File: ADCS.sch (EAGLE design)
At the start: 183 parts, among them U1 Value, U2 Value, U3 Value, U34 TMP100, U4 Value, U5 TEXAS_INSTRUMENTS-AND_GATE-SN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, U6 ISSI-DRAM-IS42S16320F-7TL, U7 TMP100, U8 BMX160, U9 BMX160, X1 ECS_INC-OSCILLATOR-ECS-400-10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, X2 BU-SMA-V, X3 2510-, X4 2510-, Y1 20MHz, Y2 20MHz

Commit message: Almost done with schematic
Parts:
- added C143, C144, C145, C146, C147, C148, C149, C150, C151, C152, C153, C154, C155, C156, C159, C162, C163, C165, C166, C168, C170, C172, C174, C175, C176, C177, C178, C179, C180, C181, C185, C187: 0.1uF, standardparts:CAPACITOR.0603
- added C157, C160, C167, C169: 2.2uF, standardparts:CAPACITOR.0603
- added C158, C161, C164: 10uF, standardparts:CAPACITOR.0805
- added C171, C173, C182, C186, C188: 1uF, standardparts:CAPACITOR.0603
- added C183: 4.7uF, standardparts:CAPACITOR.0603
- added C184: (no value), standardparts:CAPACITOR.0603
- added C189: 10nF, standardparts:CAPACITOR.0603
- added IC1: XC9572XL-10VQG44C, SamacSys_Parts:XC9572XL-10VQG44C
- added J1: SEAF-10-XX.X-XX-04-X-A, SEAF-10-XX.X-XX-04-X-A:SEAF-10-XX.X-XX-04-X-A
- added JP1, JP4: (no value), pinhead:PINHD-1X8
- added JP5, JP6, JP7, JP8: (no value), pinhead:PINHD-1X2
- added JP9: (no value), pinhead:PINHD-1X4
- added R13, R21, R30, R32, R40, R62, R63: 10k, standardparts:RESISTOR.0603
- added R14, R22, R42: (no value), standardparts:RESISTOR.0603
- added R15, R16, R17, R18, R23, R24, R25, R26, R37, R39, R44, R45, R46, R47, R48, R49, R50, R51, R53, R54, R55, R56, R57, R58, R59, R60: DNI, standardparts:RESISTOR.0603
- added R19, R20, R27, R28: 1R_1%, standardparts:RESISTOR.0603
- added R29, R31: (no value), standardparts:RESISTOR.1206
- added R36, R38, R52, R61: 4.7k, standardparts:RESISTOR.0603
- added R41: 120R, standardparts:RESISTOR.0603
- added R43: 1M, standardparts:RESISTOR.0603
- added U10, U11: Value, Module_ICs:TEXAS_INSTRUMENTS-MOTOR_PWM_DRIVER-DRV8833CPWP
- added U12, U13: TEXAS_INSTRUMENTS-CURRENT_MONITOR-INA226_DGS_10, Module_Regulators:TEXAS_INSTRUMENTS-CURRENT_MONITOR-INA226_DGS_10
- added U14: Value, Module_ICs:TEXAS_INSTRUMENTS-CAN_TRANSCEIVER-TCAN1042VDRQ1
- added U15, U16: KIOXIA_AMERICA-NAND_FLASH-TC58CVG0S3HRAIG, Module_ICs:KIOXIA_AMERICA-NAND_FLASH-TC58CVG0S3HRAIG
- added X5: 2510-, con-3m:2510-
- R4: value 10k -> 4.7k
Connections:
- removed net I2C0_SCL: U34.SCL, U7.SCL, U8.SCX, U9.SCX
- removed net I2C0_SDA: U34.SDA, U7.SDA, U8.SDX, U9.SDX
- new net !ADCS_FAILURE: C184.1, IC1.I/O_1, R42.2
- new net !COMMS1_ERROR: IC1.I/O_9
- new net !COMMS1_NAND_CS: U15.!CS, U3.PF3
- new net !COMMS1_RESET: IC1.I/O_3
- new net !COMMS1_UNRESPONSIVE: IC1.I/O_11, R62.2, U2D.GPIO20
- new net !COMMS2_ERROR: IC1.I/O_10
- new net !COMMS2_RESET: IC1.I/O_4
- new net !COMMS2_UNRESPONSIVE: IC1.I/O_12, R63.2, U2D.GPIO21
- new net !COMMS_ERROR: R61.2, U3.PD6
- new net !MTQ12_FAULT: R14.2, U10.FAULT_N
- new net !MTQ12_SLEEP: R13.2, U10.SLEEP_N
- new net !MTQ34_FAULT: R22.2, U11.FAULT_N
- new net !MTQ34_SLEEP: R21.2, U11.SLEEP_N
- new net !SMC_NAND_CS: U16.!CS, U2D.GPIO19
- new net ADCS_ERROR: IC1.I/O_6, J1G$3.10
- new net ADCS_FAILURE: J1G$1.10
- new net ADCS_ONLINE: IC1.I/O_5, J1G$3.9
- new net ADC_A0: C149.1, JP1.2, U2B.ADCINA0_DACOUTA
- new net ADC_A1: C148.1, JP1.3, U2B.ADCINA1_DACOUTB
- new net ADC_A2: C147.1, JP1.4, U2B.ADCINA2_CMPIN1P
- new net ADC_A3: C146.1, JP1.5, U2B.ADCINA3_CMPIN1N
- new net ADC_A4: C145.1, JP1.6, U2B.ADCINA4_CMPIN2P
- new net ADC_A5: C144.1, JP1.7, U2B.ADCINA5_CMPIN2N
- new net ADC_B0: C156.1, JP4.2, U2B.ADCINB0_VDAC
- new net ADC_B1: C155.1, JP4.3, U2B.ADCINB1_DACOUTC
- new net ADC_B2: C154.1, JP4.4, U2B.ADCINB2_CMPIN3P
- new net ADC_B3: C153.1, JP4.5, U2B.ADCINB3_CMPIN3N
- new net ADC_B4: C152.1, JP4.6, U2B.ADCINB4
- new net ADC_B5: C151.1, JP4.7, U2B.ADCINB5
- new net COMMS1_NAND_MISO: U15.SO/SO1, U3.PF0
- new net COMMS1_NAND_MOSI: U15.SI/SO0, U3.PF1
- new net COMMS1_NAND_SCK: U15.SCK, U3.PF2
- new net COMMS1_NMI: C189.1, IC1.I/O_7, R52.1, U3.PD7
- new net COMMS2_NMI: IC1.I/O_8
- new net COMMS2_UART_RX: J1G$3.8
- new net COMMS2_UART_TX: J1G$3.7
- new net CPLD_I1: IC1.I/O/GTS1, J1G$4.3
- new net CPLD_I2: IC1.I/O_23, J1G$4.4
- new net CPLD_I3: IC1.I/O_24, J1G$4.5
- new net CPLD_I4: IC1.I/O_25, J1G$4.6
- new net CPLD_O1: IC1.I/O_26, J1G$4.7
- new net CPLD_O2: IC1.I/O_27, J1G$4.8
- new net CPLD_O3: IC1.I/O_28, J1G$4.9
- new net CPLD_O4: IC1.I/O/GCK1, J1G$4.10
- new net EPWM1A: R18.1, U10.AIN1, U2D.GPIO0
- new net EPWM1B: R17.1, U10.AIN2, U2D.GPIO1
- new net EPWM2A: R16.1, U10.BIN1, U2D.GPIO2
- new net EPWM2B: R15.1, U10.BIN2, U2D.GPIO3
- new net EPWM3A: R26.1, U11.AIN1, U2D.GPIO4
- new net EPWM3B: R25.1, U11.AIN2, U2D.GPIO5
- new net EPWM4A: R24.1, U11.BIN1, U2D.GPIO6
- new net EPWM4B: R23.1, U11.BIN2, U2D.GPIO7
- new net MTQ1_OUT1: JP5.1, U10.AOUT1
- new net MTQ1_OUT2: JP5.2, U10.AOUT2
- new net MTQ2_OUT1: JP6.1, U10.BOUT1
- new net MTQ2_OUT2: JP6.2, U10.BOUT2
- new net MTQ3_OUT1: JP7.1, U11.AOUT1
- new net MTQ3_OUT2: JP7.2, U11.AOUT2
- new net MTQ4_OUT1: JP8.1, U11.BOUT1
- new net MTQ4_OUT2: JP8.2, U11.BOUT2
- new net MTQ_12_ALERT: R32.2, U13.ALERT
- new net MTQ_12_VCC: C158.1, C159.1, C164.1, C165.1, R31.2, U10.VM, U13.VIN-
- new net MTQ_34_ALERT: R30.2, U12.ALERT
- new net MTQ_34_VCC: C161.1, C162.1, R29.2, U11.VM, U12.VIN-
- new net N$10: C157.1, U10.VINT
- new net N$12: R19.1, U10.AISEN
- new net N$13: R20.1, U10.BISEN
- new net N$14: C160.1, U11.VINT
- new net N$15: R27.1, U11.AISEN
- new net N$16: R28.1, U11.BISEN
- new net N$17: R44.2, R45.1, U15.!WP!/SO2
- new net N$18: IC1.TMS, X5-2.KL
- new net N$19: IC1.TCK, X5-4.KL
- new net N$29: IC1.TDI, X5-8.KL
- new net N$30: IC1.TDO, X5-6.KL
- new net N$37: R48.2, R49.1, U16.!WP!/SO2
- new net N$38: R46.2, R47.1, U15.!HOLD!/SO3
- new net N$39: R50.2, R51.1, U16.!HOLD!/SO3
- new net SMC_ERR_OUT_CPLD: IC1.I/O_2, R43.2
- new net SMC_I2C0_SCL: J1G$1.2, R37.2, U12.SCL, U13.SCL, U2F.GPIO105, U34.SCL, U7.SCL, U8.SCX, U9.SCX
- new net SMC_I2C0_SDA: J1G$1.1, R36.2, U12.SDA, U13.SDA, U2F.GPIO104, U34.SDA, U7.SDA, U8.SDX, U9.SDX
- new net SMC_I2C1_SCL: J1G$1.5, R39.2, U2D.GPIO41
- new net SMC_I2C1_SDA: J1G$1.4, R38.2, U2D.GPIO40
- new net SMC_MCAN_RX: U14.RXD, U2D.GPIO10
- new net SMC_MCAN_STB: R40.1, U14.STB, U2D.GPIO9
- new net SMC_MCAN_TX: U14.TXD, U2D.GPIO8
- new net SMC_NAND_MISO: U16.SO/SO1, U2D.GPIO17
- new net SMC_NAND_MOSI: U16.SI/SO0, U2D.GPIO16
- new net SMC_NAND_SCK: U16.SCK, U2D.GPIO18
- new net SMC_UART0_RX: J1G$3.2, JP9.3, U2E.GPIO43
- new net SMC_UART0_TX: J1G$3.1, JP9.2, U2E.GPIO42
- net !GLOBAL_RESET: now also IC1.I/O/GCK2
- net BMX160_1_INT1: now also R54.2, R55.1, U2D.GPIO11
- net BMX160_1_INT2: now also R53.2, R56.1, U2D.GPIO12
- net BMX160_2_INT1: now also R58.2, R59.1, U2D.GPIO13
- net BMX160_2_INT2: now also R57.2, R60.1, U2D.GPIO14
- net CANH: now also J1G$1.7, R41.1, U14.CANH
- net CANL: now also J1G$1.8, R41.2, U14.CANL
- net COMMS1_UART_RX: now also J1G$3.5
- net COMMS1_UART_TX: now also J1G$3.4
- net SMC_ERR_OUT: now also R43.1
- net VCC_3V3_IO: now also C143.1, C150.1, C163.1, C166.1, C167.1, C170.1, C171.1, C172.1, C175.1, C176.1, C177.1, C178.1, C179.1, C180.1, C181.1, C182.1, C183.1, C185.1, C186.1, C187.1, C188.1, IC1.VCCINT_3.3V_1, IC1.VCCINT_3.3V_2, IC1.VCCIO_2.5V/3.3V, J1G$2.3, J1G$2.4, JP1.1, JP4.1, JP9.1, R13.1, R14.1, R21.1, R22.1, R30.1, R32.1, R36.1, R37.1, R38.1, R39.1, R42.1, R44.1, R46.1, R48.1, R50.1, R53.1, R54.1, R57.1, R58.1, R61.1, R62.1, R63.1, U12.VS, U13.A0, U13.VS, U14.VIO, U15.VCC, U16.VCC, X5-1.KL
- net VCC_5V0: now also C168.1, C169.1, C173.1, C174.1, J1G$2.1, J1G$2.2, R29.1, R31.1, U12.VBUS, U12.VIN+, U13.VBUS, U13.VIN+, U14.VCC
- net VSS: now also C143.2, C144.2, C145.2, C146.2, C147.2, C148.2, C149.2, C150.2, C151.2, C152.2, C153.2, C154.2, C155.2, C156.2, C157.2, C158.2, C159.2, C160.2, C161.2, C162.2, C163.2, C164.2, C165.2, C166.2, C167.2, C168.2, C169.2, C170.2, C171.2, C172.2, C173.2, C174.2, C175.2, C176.2, C177.2, C178.2, C179.2, C180.2, C181.2, C182.2, C183.2, C184.2, C185.2, C186.2, C187.2, C188.2, C189.2, IC1.GND_1, IC1.GND_2, IC1.GND_3, J1G$1.3, J1G$1.6, J1G$1.9, J1G$2.10, J1G$2.5, J1G$2.6, J1G$2.7, J1G$2.8, J1G$2.9, J1G$3.3, J1G$3.6, J1G$4.1, J1G$4.2, JP1.8, JP4.8, JP9.4, R15.2, R16.2, R17.2, R18.2, R19.2, R20.2, R23.2, R24.2, R25.2, R26.2, R27.2, R28.2, R40.2, R45.2, R47.2, R49.2, R51.2, R52.2, R55.2, R56.2, R59.2, R60.2, U10.GND, U10.PPAD, U11.GND, U11.PPAD, U12.A0, U12.A1, U12.GND, U13.A1, U13.GND, U14.GND, U15.VSS, U16.VSS, X5-3.KL, X5-5.KL, X5-9.KL
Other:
- note added: "1Gb NAND flash"
- note added: "ADC block (sun sensor and auxiliary)"
- note added: "I2C0 Address 0x40"
- note added: "I2C0 Address 0x41"

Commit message: Finished RF MUX
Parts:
- added C190: 0.1uF, standardparts:CAPACITOR.0603
- added C191, C194: 10nF, standardparts:CAPACITOR.0603
- added C192, C193: 100pF, standardparts:CAPACITOR.0603
- added L10, L11, L8: 1.2nH, standardparts:RF-INDUCTOR.0402
- added R64: 0R, standardparts:RESISTOR.0603
- added R65: 10k, standardparts:RESISTOR.0603
- added U17: QORVO-RF_SWITCH-QPC7512, Module_ICs:QORVO-RF_SWITCH-QPC7512
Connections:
- new net ANT2_PREMUX_50Z: L11.1
- new net N$40: L8.1, U17.RFC
- new net N$41: L11.2, U17.RF2
- new net N$42: L10.2, U17.RF1
- new net RF_MUX_CTRL: C193.1, C194.1, IC1.I/O_13, R65.1, U17.CTRL
- new net RF_MUX_EN: C192.1, R64.2, U17.EN
- net ANT1_PREMUX_50Z: now also L10.1
- net ANTENNA: now also L8.2
- net VCC_3V3_IO: now also C190.1, C191.1, R64.1, U17.VCC
- net VSS: now also C190.2, C191.2, C192.2, C193.2, C194.2, R65.2, U17.GND
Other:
- note added: "Note: CTRL = 1; then primary is enabled CTRL = 0; then secondary is enabled"

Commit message: Finalized schematic 11-15-20 iteration 1
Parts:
- added C195, C204, C215, C236, C238, C239, C244, C245, C252, C253, C254, C255, C264: 0.1uF, standardparts:CAPACITOR.0603
- added C196, C199, C200, C201, C202, C210: 10uF, standardparts:CAPACITOR.0805
- added C197, C211: 22uF, standardparts:CAPACITOR.0805
- added C198: DNI, standardparts:CAPACITOR.0805
- added C203, C205, C206, C231, C242: 2.2uF, standardparts:CAPACITOR.0603
- added C207: 100nF, standardparts:CAPACITOR.0805
- added C208: 47uF, standardparts:CAPACITOR.1206
- added C209: 100uF, standardparts:CAPACITOR.1206
- added C212: 0.1uF, standardparts:CAPACITOR.0805
- added C213, C214: 10pF, standardparts:CAPACITOR.0603
- added C216: 1.5nF, standardparts:CAPACITOR.0402
- added C217: 220nF, standardparts:CAPACITOR.0402
- added C218, C233: 10nF, standardparts:CAPACITOR.0402
- added C219, C220, C221, C222, C223, C224, C225, C226, C227, C228, C229: 47nF, standardparts:CAPACITOR.0402
- added C230, C248: 10uF, standardparts:CAPACITOR.0603
- added C232: 33pF, standardparts:CAPACITOR.0402
- added C234: 100pF, standardparts:CAPACITOR.0402
- added C235, C237: 0.01uF, standardparts:CAPACITOR.0603
- added C240, C241, C263: DNI, standardparts:CAPACITOR.0603
- added C243, C246, C247, C250, C251, C256, C265: 1uF, standardparts:CAPACITOR.0603
- added C249: 4.7uF, standardparts:CAPACITOR.0603
- added C257: 15pF, standardparts:CAPACITOR.0603
- added C258: 1pF, standardparts:CAPACITOR.0603
- added C259: 2.2pF, standardparts:CAPACITOR.0603
- added C260, C261: 3.3pF, standardparts:CAPACITOR.0603
- added C262: 3pF, standardparts:CAPACITOR.0603
- added C266: 10nF, standardparts:CAPACITOR.0603
- added JP10, JP11: (no value), pinhead:PINHD-1X4
- added L12: 3.3uH, Module_Inductors:EATON-INDUCTOR-HC3_3R3_R
- added L13: 10nH, standardparts:RF-INDUCTOR.0402
- added L14: 7.5nH, standardparts:RF-INDUCTOR.0603
- added L15: 18nH, standardparts:RF-INDUCTOR.0603
- added L16, L17, L19, L20: 12nH, standardparts:RF-INDUCTOR.0603
- added L18: 15nH, standardparts:RF-INDUCTOR.0603
- added R66: 0.002R, standardparts:RESISTOR.1812
- added R67, R68, R78, R82, R83, R84, R95, R96: 10k, standardparts:RESISTOR.0603
- added R69: 255k_1%, standardparts:RESISTOR.0603
- added R70: 27k_1%, standardparts:RESISTOR.0603
- added R71, R72: 100k, standardparts:RESISTOR.0603
- added R73: 51.7k, standardparts:RESISTOR.0603
- added R74: 11.5k, standardparts:RESISTOR.0603
- added R75: 24.9k, standardparts:RESISTOR.0603
- added R76: 0.1R, standardparts:RESISTOR.0603
- added R77: 56k_1%, standardparts:RESISTOR.0603
- added R79: DNI, standardparts:RESISTOR.0402
- added R80: 10R, standardparts:RESISTOR.0402
- added R81, R93, R94: 10R, standardparts:RESISTOR.0603
- added R85, R86, R87, R88, R89, R90: DNI, standardparts:RESISTOR.0603
- added R91, R92: 4.7k, standardparts:RESISTOR.0603
- added U18: TEXAS_INSTRUMENTS-CURRENT_MONITOR-INA226_DGS_10, Module_Regulators:TEXAS_INSTRUMENTS-CURRENT_MONITOR-INA226_DGS_10
- added U19: TEXAS_INSTRUMENTS-BUCK_CONVERTER-TPS53513RVER, Module_Regulators:TEXAS_INSTRUMENTS-BUCK_CONVERTER-TPS53513RVER
- added U20: Value, Module_ICs:TEXAS_INSTRUMENTS-RADAR-CC1200RHBR
- added U21: Value, Module_ICs:TEXAS_INSTRUMENTS-MICROCONTROLLER-TM4C1230D5PMI7R
- added U22: Value, Module_ICs:TEXAS_INSTRUMENTS-CAN_TRANSCEIVER-TCAN1042VDRQ1
- added U23: TEXAS_INSTRUMENTS-AND_GATE-SN74LVC1G11_DCK_6, Module_Gates:TEXAS_INSTRUMENTS-AND_GATE-SN74LVC1G11_DCK_6
- added U24: KIOXIA_AMERICA-NAND_FLASH-TC58CVG0S3HRAIG, Module_ICs:KIOXIA_AMERICA-NAND_FLASH-TC58CVG0S3HRAIG
- added X6: 5566-4, con-molex:5566-4
- added X7: ECS_INC-OSCILLATOR-ECS-400-10-37-CKM-TR, Module_ICs:ECS_INC-OSCILLATOR-ECS-400-10-37-CKM-TR
- added X8: 2510-, con-3m:2510-
- added Y3: 20MHz, Module_ICs:ESC-OSCILLATOR-ECS_200_9_33B_CTP_TR
- R14, R22: value (none) -> 10k
- R29, R31: value (none) -> 0.015R
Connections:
- net !JTAG_RST renamed !COMMS1_JTAG_RST
- removed net !CC1200_1_RESET_PRE: C51.1, R34.2, U1.RESET_N
- removed net !COMMS1_SMCRESET: C3.1, R6.2, U5.A
- removed net !COMMS_ERROR: R61.2, U3.PD6
- removed net !MTQ12_FAULT: R14.2, U10.FAULT_N
- removed net !MTQ12_SLEEP: R13.2, U10.SLEEP_N
- removed net !MTQ34_FAULT: R22.2, U11.FAULT_N
- removed net !MTQ34_SLEEP: R21.2, U11.SLEEP_N
- new net !CC1200_2_RESET: C215.1, R78.2, U20.RESET_N, U21.PB7
- new net !CC1200_2_SPI_CS: U20.CS_N, U21.PA3_SSI0FSS
- new net !COMMS2_JTAG_RST: C237.1, R81.2, R83.2, U23.C
- new net !COMMS2_NAND_CS: U21.PF3, U24.!CS
- new net !MTQ_12_FAULT: R14.2, U10.FAULT_N, U2F.GPIO86
- new net !MTQ_12_SLEEP: R13.2, U10.SLEEP_N, U2F.GPIO85
- new net !MTQ_34_FAULT: R22.2, U11.FAULT_N, U2F.GPIO89
- new net !MTQ_34_SLEEP: R21.2, U11.SLEEP_N, U2F.GPIO88
- new net !SMC_UNRESPONSIVE1: IC1.I/O_18, R93.2, R95.2
- new net !SMC_UNRESPONSIVE1_PRE: R93.1, U3.PF4
- new net !SMC_UNRESPONSIVE2: IC1.I/O_17, R94.2, R96.2
- new net !SMC_UNRESPONSIVE2_PRE: R94.1, U21.PF4
- new net !TPS53513_PGOOD: R68.2, R71.2, R72.2, U19.PGOOD
- new net CC1200_2_SPI_CLK: U20.SCLK, U21.PA2_SSI0CLK
- new net CC1200_2_SPI_MISO: U20.SO_GPIO1, U21.PA4_SSI0RX
- new net CC1200_2_SPI_MOSI: U20.SI, U21.PA5_SSI0TX
- new net COMMS2_CAN_RX: U21.PB4, U22.RXD
- new net COMMS2_CAN_STB: U21.PB6, U22.STB
- new net COMMS2_CAN_TX: U21.PB5, U22.TXD
- new net COMMS2_I2C0_SCL: JP10.3, U21.PB2_I2C0SCL
- new net COMMS2_I2C0_SDA: JP10.2, U21.PB3_I2C0SDA
- new net COMMS2_NAND_MISO: U21.PF0, U24.SO/SO1
- new net COMMS2_NAND_MOSI: U21.PF1, U24.SI/SO0
- new net COMMS2_NAND_SCK: U21.PF2, U24.SCK
- new net LNA2_N: C261.2, L17.1, L18.2, U20.LNA_N
- new net LNA2_P: C260.1, L18.1, L19.2, U20.LNA_P
- new net MAIN_CURRENT_ALERT: R67.2, U18.ALERT, U2D.GPIO15
- new net N$43: R69.2, R70.1, U19.RF
- new net N$44: R72.1, U2E.GPIO83
- new net N$45: IC1.I/O_14, R71.1
- new net N$46: C207.1, U19.VBST
- new net N$47: C207.2, L12.P$1, U19.SW, U19.SW_2, U19.SW_3, U19.SW_4
- new net N$48: R75.2, U19.TRIP
- new net N$49: R76.2, U19.MODE
- new net N$50: R77.1, U20.RBIAS
- new net N$51: C213.1, U20.XOSC_Q1, X7.XO
- new net N$52: C214.1, U20.XOSC_Q2, X7.XI
- new net N$53: C216.1, U20.LPF1
- new net N$54: C216.2, U20.LPF0
- new net N$55: C220.2, U20.DCPL_PFD_CHP
- new net N$56: C219.2, R79.2, U20.DCPL_XOSC
- new net N$57: C218.2, U20.DCPL_VCO
- new net N$58: C217.2, U20.DCPL
- new net N$59: C232.2, L13.2, R80.2
- new net N$60: R81.1, X8-10.KL
- new net N$61: C235.1, R84.2, U21.RST_N, U23.Y
- new net N$62: U21.PC2_TDI, X8-8.KL
- new net N$63: U21.PC3_TDO_SWO, X8-6.KL
- new net N$64: U21.PC1_TMS_SWDIO, X8-2.KL
- new net N$65: U21.PC0_TCK_SWCLK, X8-4.KL
- new net N$66: C242.1, C243.1, C244.1, C245.1, U21.VDDC, U21.VDDC_2
- new net N$67: U21.OSC0, Y3.XI
- new net N$68: U21.OSC1, Y3.XO
- new net N$69: C257.2, C258.1, L14.1
- new net N$70: C258.2, C259.1, L14.2, L15.1
- new net N$71: C260.2, L16.1, L17.2
- new net N$72: C262.1, C263.1, L15.2, L20.1
- new net N$73: R87.2, R88.1, U24.!WP!/SO2
- new net N$74: R89.2, R90.1, U24.!HOLD!/SO3
- new net TPS53513_FB: R73.2, R74.1, U19.FB
- new net TPS53513_VREG: C206.1, R69.1, R76.1, U19.VREG
- new net TRX2_SW: C259.2, L16.2, U20.TRX_SW
- new net VINPUT: C198.1, R66.1, U18.VBUS, U18.VIN+, X6-1.S, X6-2.S
- net !CC1200_1_RESET: now also C51.1, R34.2, U1.RESET_N
- net !COMMS1_ERROR: now also R61.2, U3.PD6
- net !COMMS1_RESET: now also C3.1, R6.2, U5.A
- net !COMMS2_ERROR: now also R92.2, U21.PD6
- net !COMMS2_RESET: now also C240.1, R82.2, U23.A
- net !GLOBAL_RESET: now also C241.1, R86.2, U23.B
- net ANT2_PREMUX_50Z: now also C263.2, L20.2
- net CANH: now also R85.1, U22.CANH
- net CANL: now also R85.2, U22.CANL
- net COMMS2_NMI: now also C266.1, R91.1, U21.PD7
- net COMMS2_UART_RX: now also JP11.2, U21.PA0_U0RX
- net COMMS2_UART_TX: now also JP11.3, U21.PA1_U0TX
- net MTQ_12_ALERT: now also U2F.GPIO84
- net MTQ_34_ALERT: now also U2F.GPIO87
- net PA: now also C257.1, L13.1, U20.PA
- net SMC_I2C0_SCL: now also U18.SCL
- net SMC_I2C0_SDA: now also U18.A0, U18.SDA
- net VCC_3V3_IO: now also C195.1, C208.1, C209.1, C210.1, C211.1, C212.1, C221.1, C222.1, C223.1, C224.1, C225.1, C226.1, C227.1, C228.1, C229.1, C230.1, C231.1, C232.1, C233.1, C234.1, C236.1, C238.1, C246.1, C247.1, C248.1, C249.1, C250.1, C251.1, C252.1, C253.1, C254.1, C255.1, C256.1, C264.1, C265.1, JP10.1, JP11.1, L12.P$2, R67.1, R68.1, R73.1, R78.1, R79.1, R80.1, R82.1, R83.1, R84.1, R86.1, R87.1, R89.1, R92.1, R95.1, R96.1, U18.VS, U19.VO, U20.AVDD_IF, U20.AVDD_PFD_CHP, U20.AVDD_RF, U20.AVDD_SYNTH1, U20.AVDD_SYNTH2, U20.AVDD_XOSC, U20.DVDD, U20.DVDD_2, U20.VDD_GUARD, U21.VDD, U21.VDDA, U21.VDD_2, U21.VDD_3, U21.VDD_4, U22.VIO, U23.VCC, U24.VCC, X8-1.KL
- net VCC_5V0: now also C196.1, C197.1, C199.1, C200.1, C201.1, C202.1, C203.1, C204.1, C205.1, C239.1, R66.2, U18.VIN-, U19.EN, U19.VDD, U19.VIN, U19.VIN_2, U19.VIN_3, U22.VCC
- net VSS: now also C195.2, C196.2, C197.2, C198.2, C199.2, C200.2, C201.2, C202.2, C203.2, C204.2, C205.2, C206.2, C208.2, C209.2, C210.2, C211.2, C212.2, C213.2, C214.2, C215.2, C217.1, C218.1, C219.1, C220.1, C221.2, C222.2, C223.2, C224.2, C225.2, C226.2, C227.2, C228.2, C229.2, C230.2, C231.2, C233.2, C234.2, C235.2, C236.2, C237.2, C238.2, C239.2, C240.2, C241.2, C242.2, C243.2, C244.2, C245.2, C246.2, C247.2, C248.2, C249.2, C250.2, C251.2, C252.2, C253.2, C254.2, C255.2, C256.2, C261.1, C262.2, C264.2, C265.2, C266.2, JP10.4, JP11.4, L19.1, R70.2, R74.2, R75.1, R77.2, R88.2, R90.2, R91.2, U18.A1, U18.GND, U19.EPAD, U19.GND, U19.GND1, U19.GND2, U19.PGND, U19.PGND_2, U19.PGND_3, U19.PGND_4, U19.PGND_5, U20.EXT_XOSC, U20.GND, U21.GND, U21.GNDA, U21.GND_2, U21.GND_3, U21.GND_4, U22.GND, U23.GND, U24.VSS, X6-3.S, X6-4.S, X8-3.KL, X8-5.KL, X8-9.KL, Y3.VSS
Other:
- note added: "5V to 3.3V regulator - 97.5% efficient - 19.8W max"
- note added: "Driver 1"
- note added: "Driver 2"
- note added: "External interfacing"
- note added: "I2C0 Address 0x42"
- note added: "Input current sensor"
- note added: "JTAG interface"
- note added: "RF MUX + Antenna"
- note added: "SMC control block"

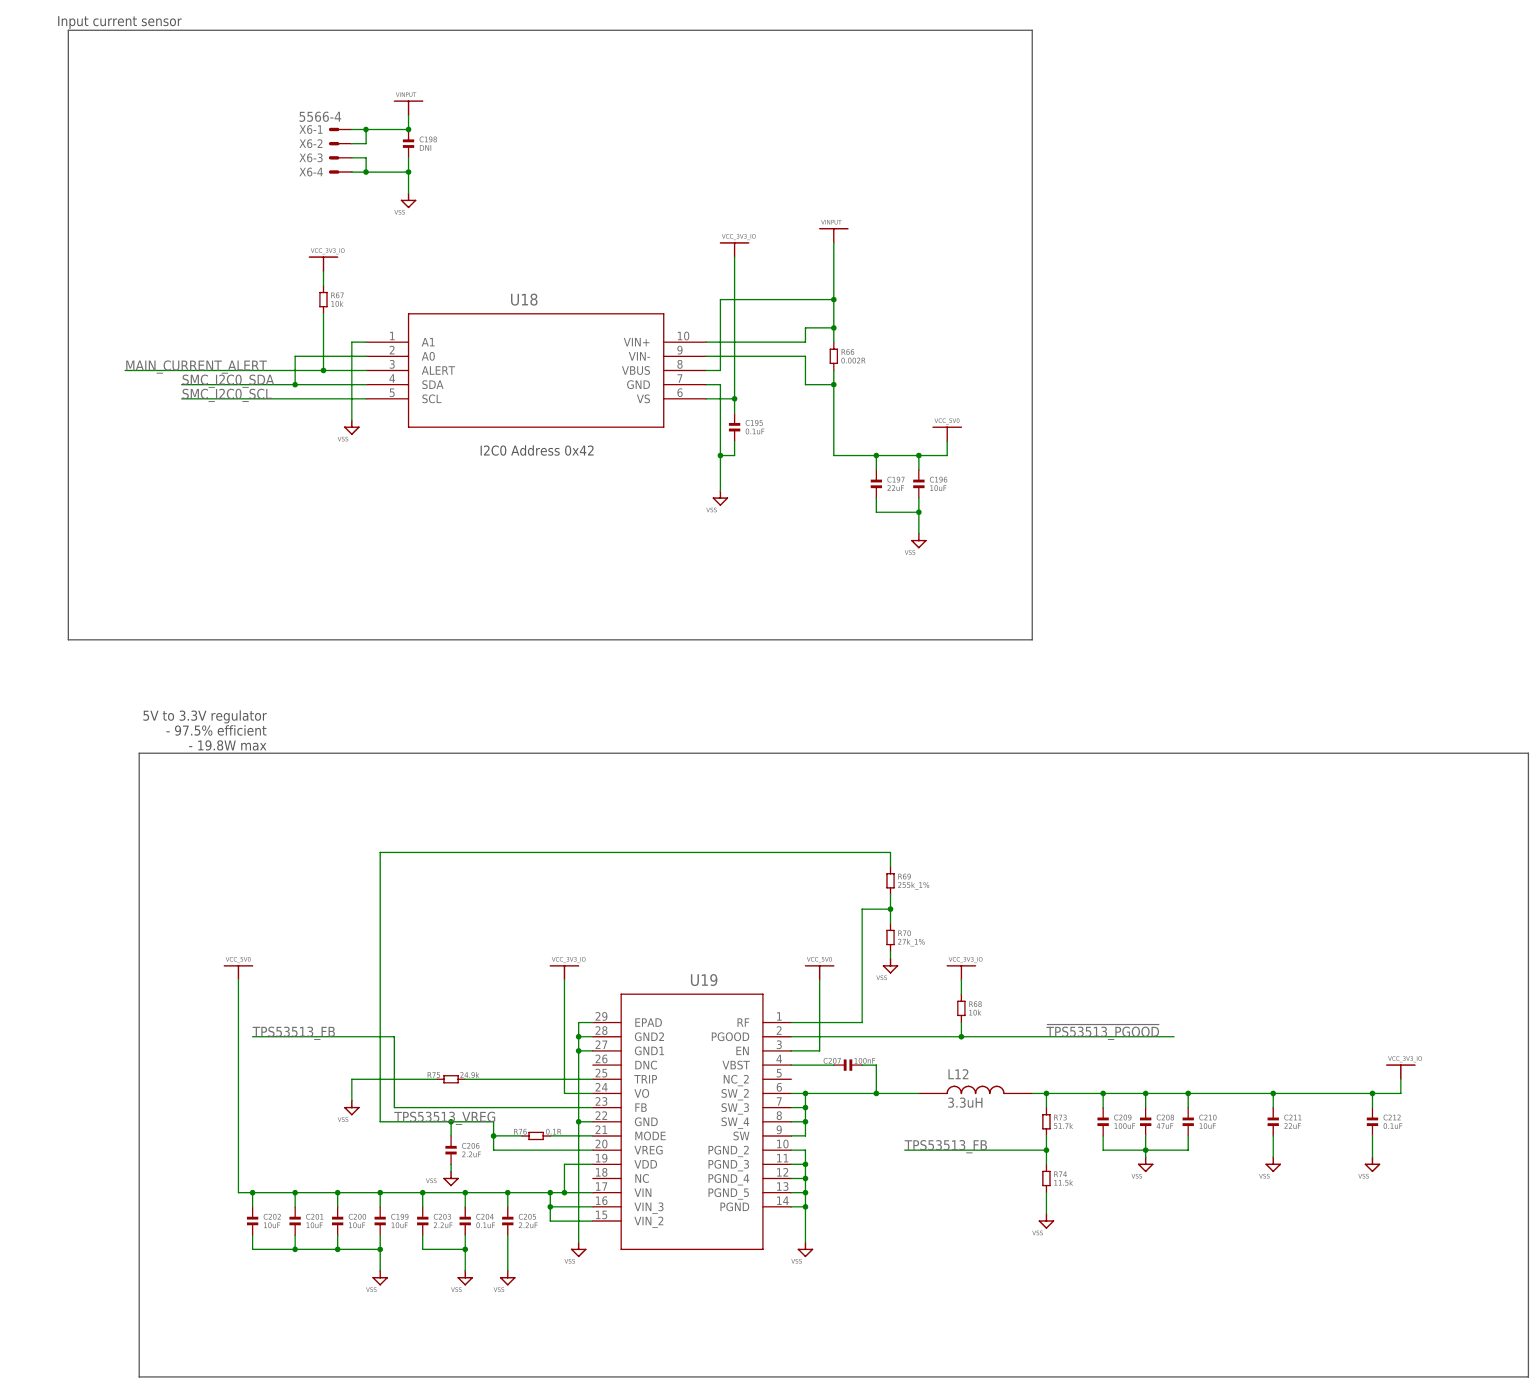
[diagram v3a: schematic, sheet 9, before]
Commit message: Added stackup and layer spec
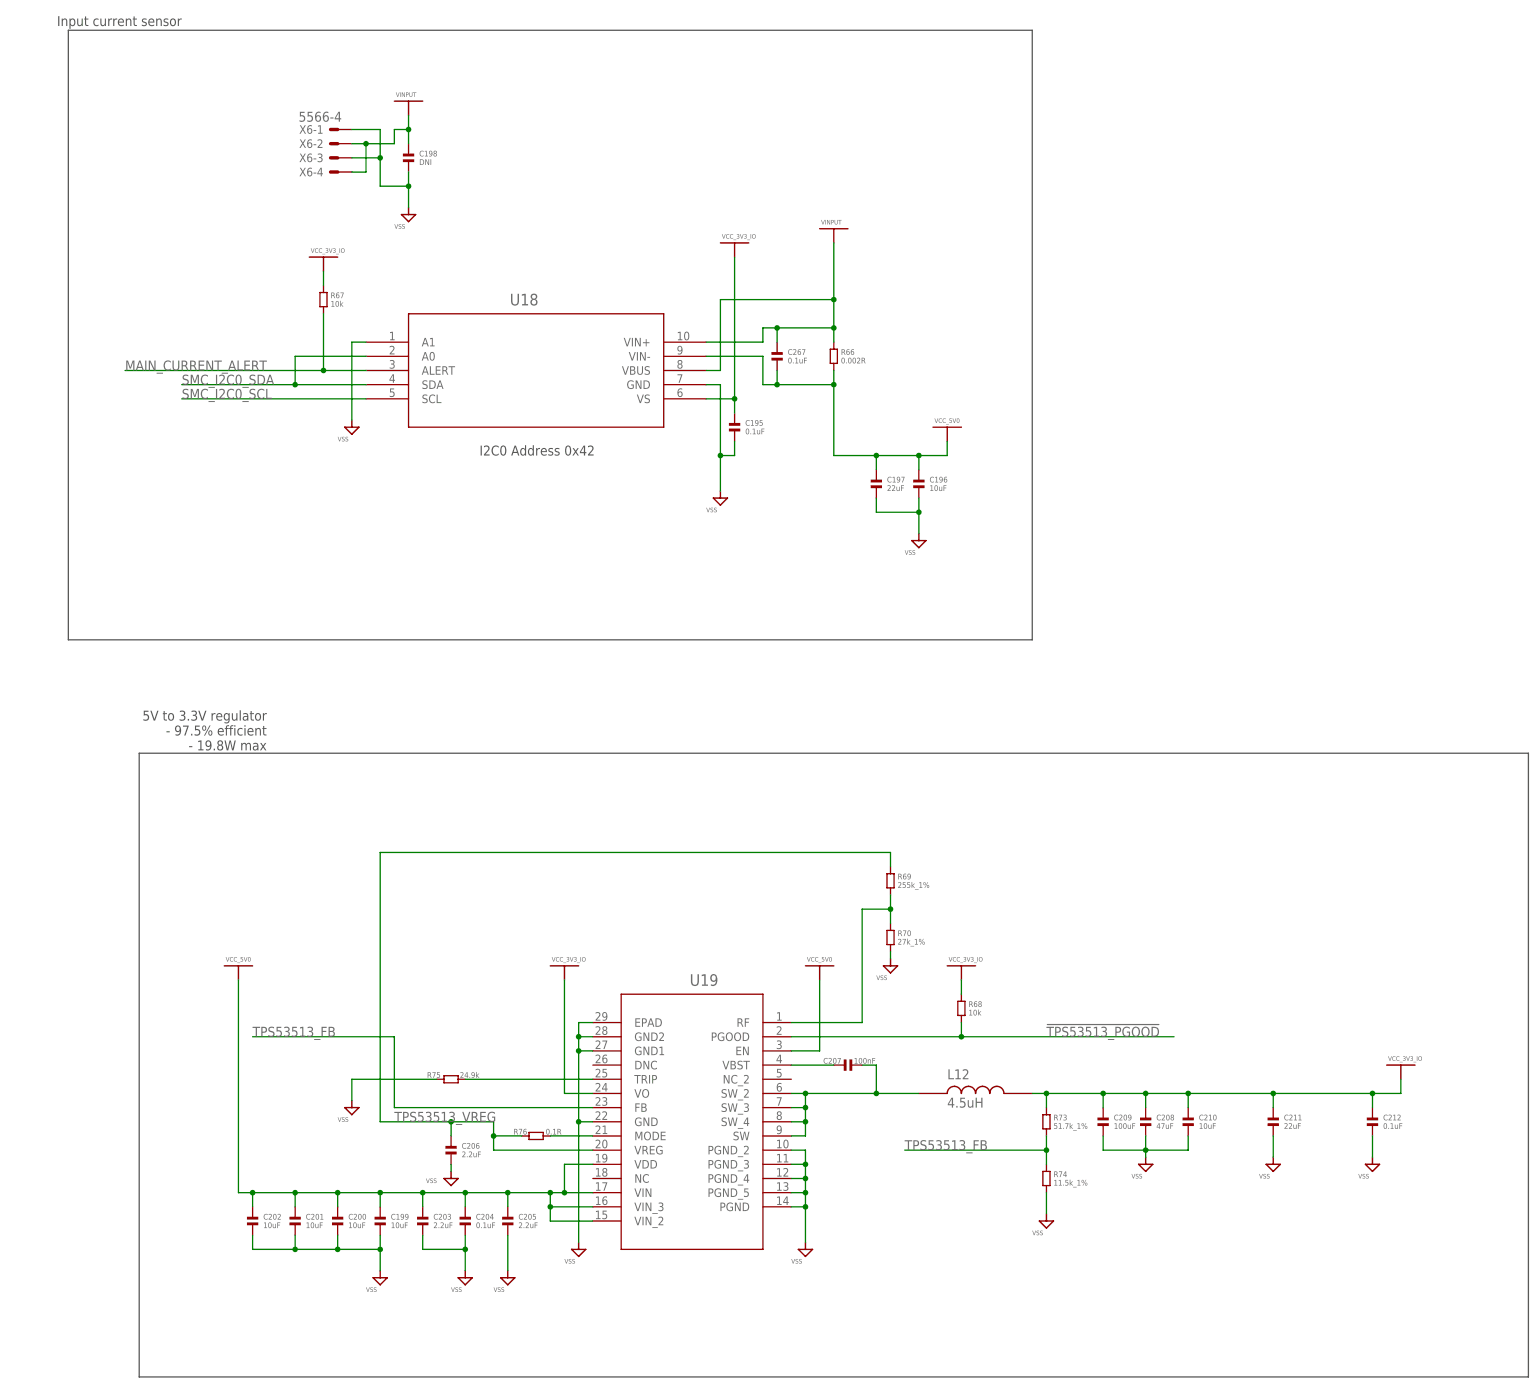
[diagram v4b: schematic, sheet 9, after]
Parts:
- added C267, C268, C269: 0.1uF, standardparts:CAPACITOR.0603
- C20, C21, C22, C23, C24, C25, C26: device standardparts:CAPACITOR.0603 -> standardparts:CAPACITOR.0402
- L1, L2, L3, L4, L5, L6, L7: device standardparts:RF-INDUCTOR.0603 -> standardparts:RF-INDUCTOR.0402
- L12: value 3.3uH -> 4.5uH; device Module_Inductors:EATON-INDUCTOR-HC3_3R3_R -> Module_Inductors:BOURNS-INDUCTOR-SRR1208-4R5ML
- R73: value 51.7k -> 51.7k_1%
- R74: value 11.5k -> 11.5k_1%
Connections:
- net MTQ_12_VCC: now also C269.2
- net MTQ_34_VCC: now also C268.2
- net VCC_5V0: now also C267.2, C268.1, C269.1
- net VINPUT: now also C267.1, X6-4.S; no longer X6-1.S
- net VSS: now also X6-1.S; no longer X6-4.S
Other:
- moved on the sheet: C198
